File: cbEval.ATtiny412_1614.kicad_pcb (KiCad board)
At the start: 2 copper layers, 35 x 109 mm, 50 parts, among them J1 Bergstik-II_3, J10 Socket.Hor.2x5.6-5535512-4, J11 Bergstik-II_3, J12 Bergstik-II_3, J13 Bergstik-II_6, J14 Bergstik-II_6, J15 Bergstik-II_6, J16 Bergstik-II_3, J17 Bergstik-II_6, J18 Bergstik-II_3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

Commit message: kleinere Änderungen
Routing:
- net /PA3: track 0.00 -> 19.0 mm
- net /PA2: track 0.00 -> 16.6 mm
- net /PA1: track 0.00 -> 13.2 mm
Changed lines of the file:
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@@
     (effects (font (size 1 1) (thickness 0.15)))
   )
+  (segment (start 144.145 93.98) (end 155.258146 93.98) (width 0.25) (layer "F.Cu") (net 43))
+  (segment (start 155.258146 93.98) (end 156.21 93.028146) (width 0.25) (layer "F.Cu") (net 43))
+  (segment (start 142.875 92.71) (end 144.145 93.98) (width 0.25) (layer "F.Cu") (net 43))
+  (segment (start 154.94 89.535) (end 154.24 89.535) (width 0.25) (layer "F.Cu") (net 43))
+  (segment (start 156.21 90.805) (end 154.94 89.535) (width 0.25) (layer "F.Cu") (net 43))
+  (segment (start 156.21 93.028146) (end 156.21 90.805) (width 0.25) (layer "F.Cu") (net 43))
+  (segment (start 142.875 90.17) (end 145.40452 92.69952) (width 0.25) (layer "F.Cu") (net 44))
+  (segment (start 155.268626 92.69952) (end 155.575 92.393146) (width 0.25) (layer "F.Cu") (net 44))
+  (segment (start 155.575 92.393146) (end 155.575 91.165) (width 0.25) (layer "F.Cu") (net 44))
+  (segment (start 145.40452 92.69952) (end 155.268626 92.69952) (width 0.25) (layer "F.Cu") (net 44))
+  (segment (start 155.215 90.805) (end 154.24 90.805) (width 0.25) (layer "F.Cu") (net 44))
+  (segment (start 155.575 91.165) (end 155.215 90.805) (width 0.25) (layer "F.Cu") (net 44))
+  (segment (start 151.11952 91.42952) (end 151.765 92.075) (width 0.25) (layer "F.Cu") (net 45))
+  (segment (start 151.765 92.075) (end 154.24 92.075) (width 0.25) (layer "F.Cu") (net 45))
+  (segment (start 146.67452 91.42952) (end 151.11952 91.42952) (width 0.25) (layer "F.Cu") (net 45))
+  (segment (start 142.875 87.63) (end 146.67452 91.42952) (width 0.25) (layer "F.Cu") (net 45))
 )

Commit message: BOM erstellt und kleinere Korrekturen
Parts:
- added R10: 10k, Resistor_SMD:R_0805_2012Metric, F.Cu at (145.4, 135.3)
- added R11: 10k, Resistor_SMD:R_0805_2012Metric, F.Cu at (148.0, 135.3)
- added R12: 10k, Resistor_SMD:R_0805_2012Metric, F.Cu at (131.1, 127.0)
- added R13: 10k, Resistor_SMD:R_0805_2012Metric, F.Cu at (138.4, 131.2)
- added R14: 10k, Resistor_SMD:R_0805_2012Metric, F.Cu at (139.1, 135.3)
- added R15: 10k, Resistor_SMD:R_0805_2012Metric, F.Cu at (151.8, 127.0)
- added R9: 10k, Resistor_SMD:R_0805_2012Metric, F.Cu at (142.9, 135.3)
- moved J12 1.27 mm to (142.9, 131.4)
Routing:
- net /PA4: track 0.00 -> 18.9 mm
- net PB3: track 0.00 -> 8.26 mm
- net /PB0: track 0.00 -> 8.26 mm
- net PB2: track 0.00 -> 7.73 mm
- net /PB1: track 0.00 -> 7.73 mm

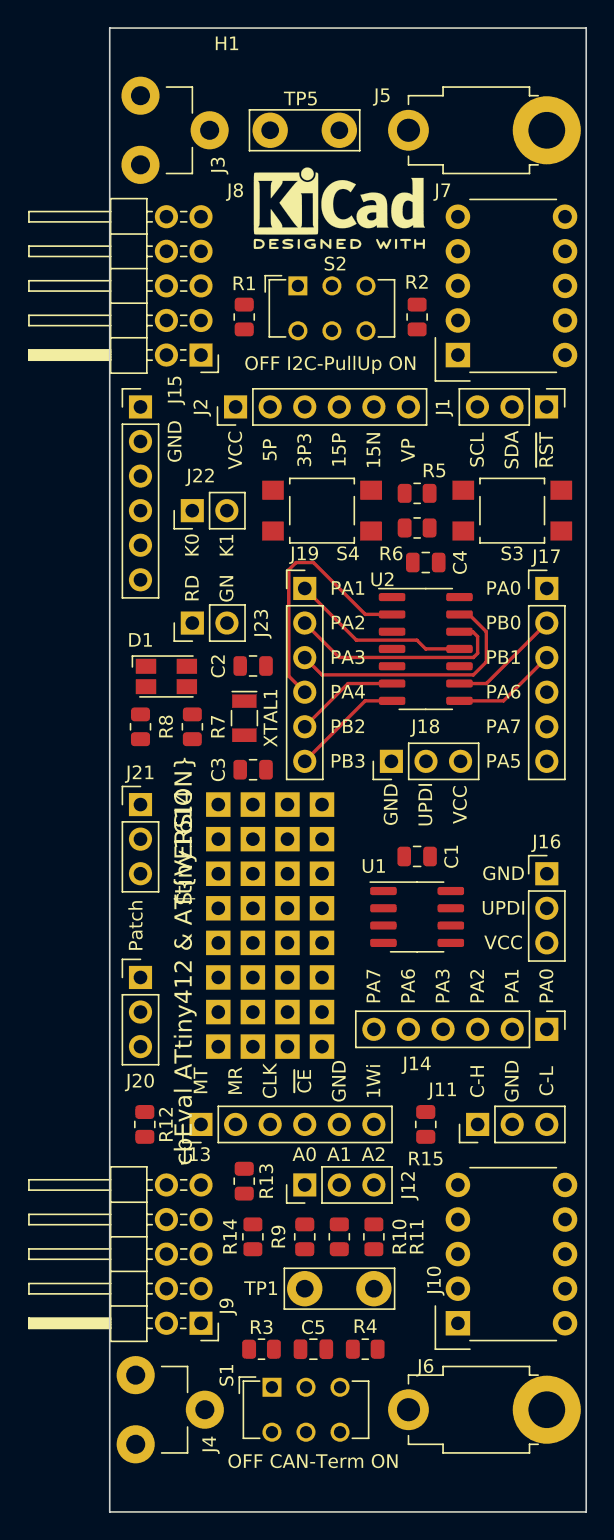
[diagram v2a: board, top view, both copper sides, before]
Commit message: Bus-Stecker ersetzt, Poti hinzugefügt
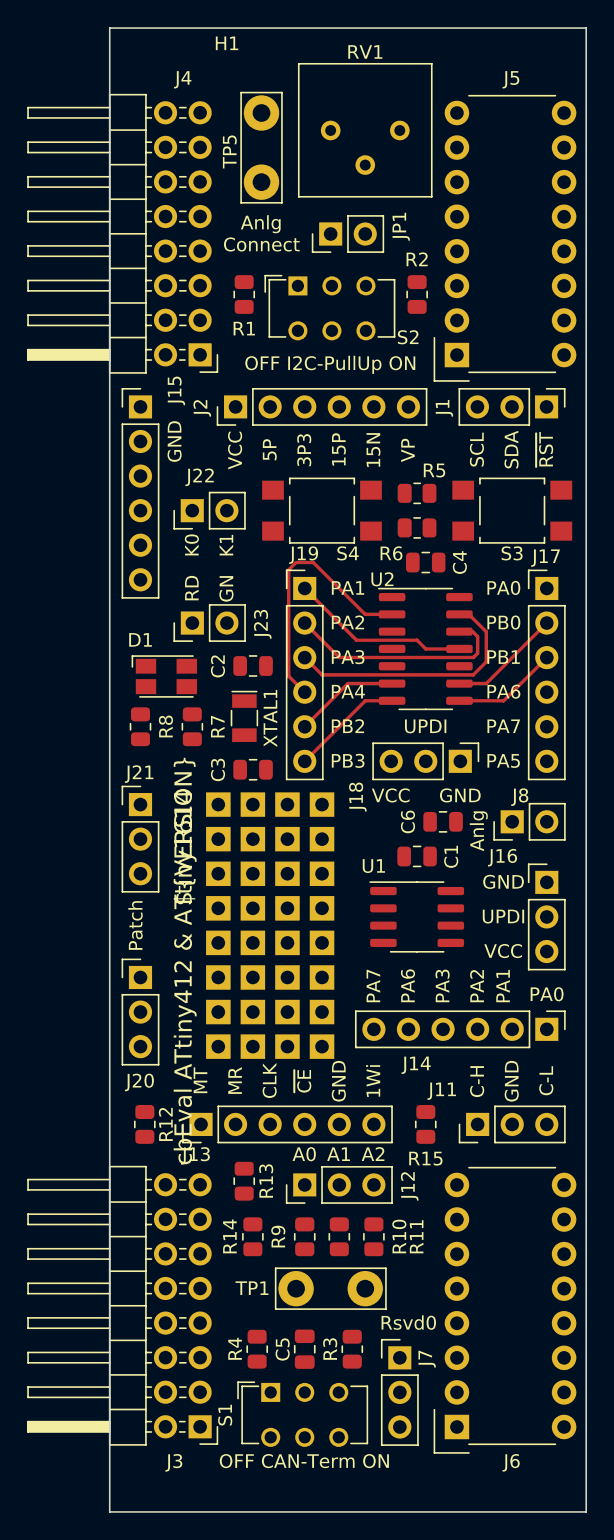
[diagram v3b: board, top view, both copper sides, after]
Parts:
- removed J10: Socket.Hor.2x5.6-5535512-4, BTech.Connector.AMPMODU-ModII:Socket.Hor.2x5.6-5535512-4
- removed J9: Header.Hor.2x5.9-103326-0-05, Connector_PinHeader_2.54mm:PinHeader_2x05_P2.54mm_Horizontal
- removed MP1: KiCAD-Logo2.5mm.SilkScreen, Symbol:KiCad-Logo2_5mm_SilkScreen
- added C6: 33n, Capacitor_SMD:C_0805_2012Metric, F.Cu at (153.0, 104.8)
- added JP1: Bergstik-II_2, Connector_PinHeader_2.54mm:PinHeader_1x02_P2.54mm_Vertical, F.Cu at (144.8, 61.6)
- added RV1: 4k7, Potentiometer_THT:Potentiometer_Bourns_3386P_Vertical, F.Cu at (144.8, 54.0)
- J3, J4: value Keystone.4918 -> Header.Hor.2x8.9-103326-0-08; footprint BTech.Connector.QuickConnect:Keystone.4918 -> Connector_PinHeader_2.54mm:PinHeader_2x08_P2.54mm_Horizontal
- J5, J6: value Keystone.3571 -> Socket.Hor.2x8.1-5535512-8; footprint BTech.Connector.QuickConnect:Keystone.3571 -> BTech.Connector.AMPMODU-ModII:Socket.Hor.2x5.6-5535512-4
- J7: value Socket.Hor.2x5.6-5535512-4 -> Bergstik-II_3; footprint BTech.Connector.AMPMODU-ModII:Socket.Hor.2x5.6-5535512-4 -> Connector_PinHeader_2.54mm:PinHeader_1x03_P2.54mm_Vertical
- J8: value Header.Hor.2x5.9-103326-0-05 -> Bergstik-II_2; footprint Connector_PinHeader_2.54mm:PinHeader_2x05_P2.54mm_Horizontal -> Connector_PinHeader_2.54mm:PinHeader_1x02_P2.54mm_Vertical
- moved J3 95.3 mm to (135.2, 149.2), turned to 180 degrees
- moved J7 79.7 mm to (149.9, 144.1)
- moved J4 77.6 mm to (135.2, 70.5), turned to 180 degrees
- moved J8 41.2 mm to (158.1, 104.8), turned to 90 degrees
- moved J5 10.9 mm to (161.9, 62.9)
- moved J6 8.98 mm to (161.9, 141.6)
- moved R4 7.94 mm to (139.4, 143.5), turned to -90 degrees
- moved R3 6.67 mm to (146.4, 143.5), turned to -90 degrees
- moved TP5 5.85 mm to (139.7, 52.7), turned to -90 degrees
- moved J18 5.06 mm to (154.3, 100.3), turned to -90 degrees
- moved R1 1.65 mm to (138.4, 66.0)
- moved R2 1.65 mm to (151.1, 66.0)
- moved J16 0.64 mm to (160.7, 109.2)
- moved C5 0.63 mm to (142.9, 143.5), turned to -90 degrees
- moved TP1 0.63 mm to (142.2, 139.1)
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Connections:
- J1 pad 1: /~RESET -> +VDC
- J4 pad 1: GND -> VCC
- J5 pad 1: GND -> VCC
- J7 pad 1: VCC -> /Reserved0
- J7 pad 2: VCC -> GND
- J7 pad 3: +5V -> /Reserved1
- J8 pad 1: VCC -> Net-(J8-Pad1)
- J8 pad 2: VCC -> Net-(J8-Pad1)
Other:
- board text added: "Anlg"
- board text added: "Anlg Connect"
- board text added: "Rsvd0"

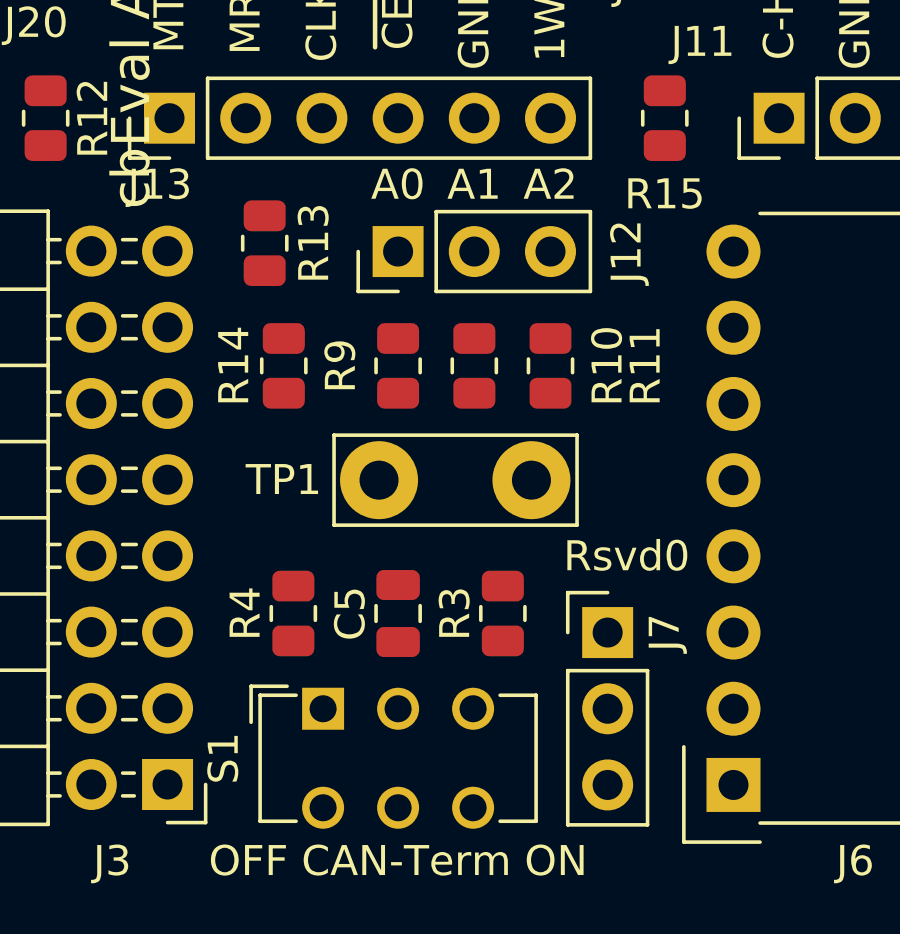
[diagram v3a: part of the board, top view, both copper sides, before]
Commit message: 1Wire-Terminierung hinzugefügt, BOM erneuert
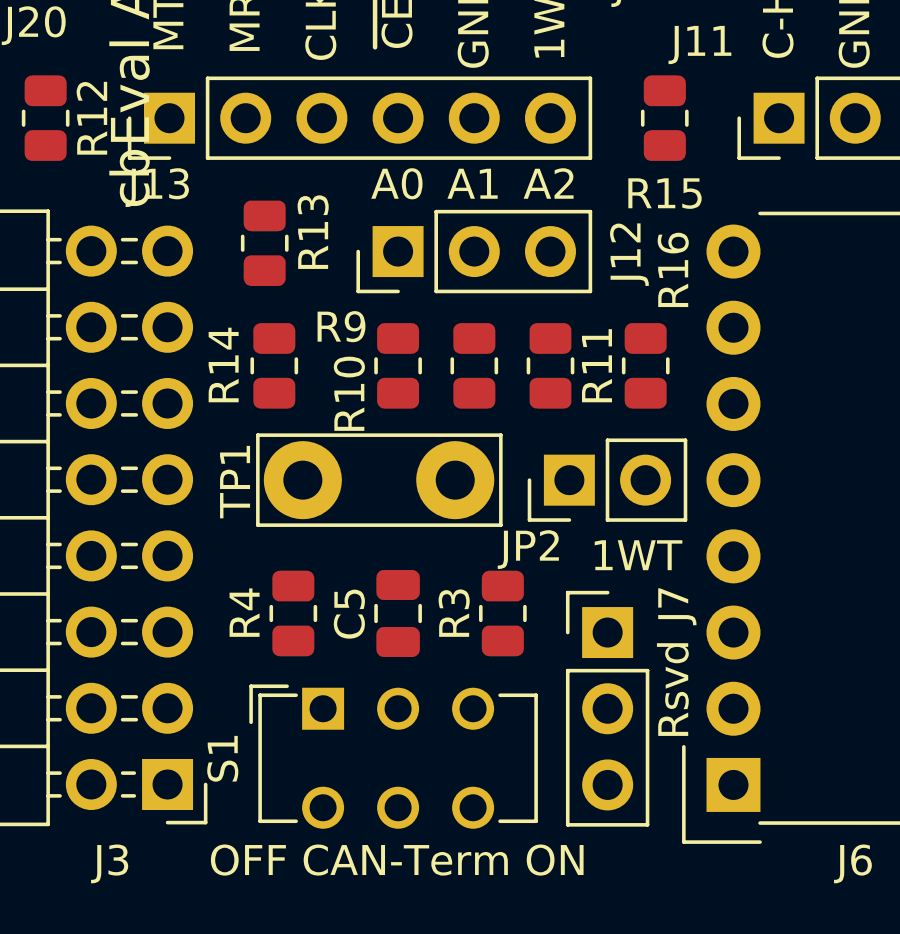
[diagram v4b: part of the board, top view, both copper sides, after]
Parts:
- added JP2: Bergstik-II_2, Connector_PinHeader_2.54mm:PinHeader_1x02_P2.54mm_Vertical, F.Cu at (148.6, 139.1)
- added R16: 4k7, Resistor_SMD:R_0805_2012Metric, F.Cu at (151.1, 135.3)
- moved TP1 2.54 mm to (139.7, 139.1)
- moved R14 0.32 mm to (138.7, 135.3)
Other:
- board text added: "1WT"
- board text added: "Rsvd"
- board text removed: "Rsvd0"
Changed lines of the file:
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@@
   (net 55 "Net-(J22-Pad2)")
   (net 56 "/Reserved0")
-  (net 57 "Net-(J8-Pad1)")
+  (net 57 "Net-(C6-Pad1)")
   (net 58 "Net-(JP1-Pad1)")
+  (net 59 "Net-(JP2-Pad2)")
   (footprint "BTech.Housing:Camdenboss.CIME.E.BE3500S.1x" locked (layer "F.Cu")
     (at 146.05 100.965)
@@
   )
   (footprint "Resistor_SMD:R_0805_2012Metric" (layer "F.Cu")
-    (at 139.065 135.255 90)
+    (at 138.7475 135.255 90)
     (descr "Resistor SMD 0805 (2012 Metric), square (rectangular) end terminal, IPC_7351 nominal, (Body size source: IPC-SM-782 page 72, https://www.pcb-3d.com/wordpress/wp-content/uploads/ipc-sm-782a_amendment_1_and_2.pdf), generated with kicad-footprint-generator")
     (tags "resistor")
@@
     (property "Tolerance" "1%")
     (attr smd)
-    (fp_text reference "R9" (at 0 1.905 90) (layer "F.SilkS")
+    (fp_text reference "R9" (at -1.27 1.905 180) (layer "F.SilkS")
       (effects (font (size 1 1) (thickness 0.15)))
     )
@@
     )
   )
+  (footprint "Resistor_SMD:R_0805_2012Metric" (layer "F.Cu")
+    (at 151.13 135.255 90)
+    (descr "Resistor SMD 0805 (2012 Metric), square (rectangular) end terminal, IPC_7351 nominal, (Body size source: IPC-SM-782 page 72, https://www.pcb-3d.com/wordpress/wp-content/uploads/ipc-sm-782a_amendment_1_and_2.pdf), generated with kicad-footprint-generator")
+    (tags "resistor")
+    (property "ID" "RC0805FR-074K7L")
+    (property "Package" "0805")
+    (property "Power" "0W125")
+    (property "Sheetfile" "cbEval.ATtiny412_1614.kicad_sch")
+    (property "Sheetname" "")
+    (property "TK" "TK100")
+    (property "Tolerance" "1%")
+    (attr smd)
+    (fp_text reference "R16" (at 3.175 0.9525 90) (layer "F.SilkS")
+      (effects (font (size 1 1) (thickness 0.15)))
+    )
+    (fp_text value "4k7" (at 0 1.65 90) (layer "F.Fab") hide
+      (effects (font (size 1 1) (thickness 0.15)))
+    )
+    (fp_text user "${REFERENCE}" (at 0 0 90) (layer "F.Fab")
+      (effects (font (size 0.5 0.5) (thickness 0.08)))
+    )
+    (fp_line (start -0.227064 -0.735) (end 0.227064 -0.735) (layer "F.SilkS") (width 0.12))
+    (fp_line (start -0.227064 0.735) (end 0.227064 0.735) (layer "F.SilkS") (width 0.12))
+    (fp_line (start -1.68 0.95) (end -1.68 -0.95) (layer "F.CrtYd") (width 0.05))
+    (fp_line (start 1.68 0.95) (end -1.68 0.95) (layer "F.CrtYd") (width 0.05))
+    (fp_line (start 1.68 -0.95) (end 1.68 0.95) (layer "F.CrtYd") (width 0.05))
+    (fp_line (start -1.68 -0.95) (end 1.68 -0.95) (layer "F.CrtYd") (width 0.05))
+    (fp_line (start -1 -0.625) (end 1 -0.625) (layer "F.Fab") (width 0.1))
+    (fp_line (start 1 -0.625) (end 1 0.625) (layer "F.Fab") (width 0.1))
+    (fp_line (start -1 0.625) (end -1 -0.625) (layer "F.Fab") (width 0.1))
+    (fp_line (start 1 0.625) (end -1 0.625) (layer "F.Fab") (width 0.1))
+    (pad "1" smd roundrect (at -0.9125 0 90) (locked) (size 1.025 1.4) (layers "F.Cu" "F.Paste" "F.Mask") (roundrect_rratio 0.243902)
+      (net 59 "Net-(JP2-Pad2)") (pintype "passive"))
+    (pad "2" smd roundrect (at 0.9125 0 90) (locked) (size 1.025 1.4) (layers "F.Cu" "F.Paste" "F.Mask") (roundrect_rratio 0.243902)
+      (net 7 "/One-Wire") (pintype "passive"))
+    (model "${KICAD6_3DMODEL_DIR}/Resistor_SMD.3dshapes/R_0805_2012Metric.wrl"
+      (offset (xyz 0 0 0))
+      (scale (xyz 1 1 1))
+      (rotate (xyz 0 0 0))
+    )
+  )
   (footprint "Connector_PinHeader_2.54mm:PinHeader_1x02_P2.54mm_Vertical" (layer "F.Cu")
     (at 144.78 61.595 90)
@@
       (net 58 "Net-(JP1-Pad1)") (pinfunction "A") (pintype "passive"))
     (pad "2" thru_hole oval (at 0 2.54 90) (locked) (size 1.7 1.7) (drill 1) (layers *.Cu *.Mask)
-      (net 57 "Net-(J8-Pad1)") (pinfunction "B") (pintype "passive"))
+      (net 57 "Net-(C6-Pad1)") (pinfunction "B") (pintype "passive"))
     (model "${KICAD6_3DMODEL_DIR}/Connector_PinHeader_2.54mm.3dshapes/PinHeader_1x02_P2.54mm_Vertical.wrl"
       (offset (xyz 0 0 0))
@@
   )
   (footprint "TestPoint:TestPoint_Bridge_Pitch5.08mm_Drill1.3mm" (layer "F.Cu")
-    (at 142.24 139.065)
+    (at 139.7 139.065)
     (descr "wire loop as test point, pitch 5.08mm, hole diameter 1.3mm, wire diameter 1.0mm")
     (tags "test point wire loop")
@@
     (property "Usage" "Meas GND")
     (attr through_hole)
-    (fp_text reference "TP1" (at -3.175 0) (layer "F.SilkS")
+    (fp_text reference "TP1" (at -2.2225 0 90) (layer "F.SilkS")
       (effects (font (size 1 1) (thickness 0.15)))
     )
@@
     (property "Usage" "Reserved")
     (attr through_hole)
-    (fp_text reference "J7" (at 1.905 0 90) (layer "F.SilkS")
+    (fp_text reference "J7" (at 2.2225 -0.9525 270) (layer "F.SilkS")
       (effects (font (size 1 1) (thickness 0.15)))
     )
@@
     (property "Tolerance" "1%")
     (attr smd)
-    (fp_text reference "R11" (at 0 -3.175 90) (layer "F.SilkS")
+    (fp_text reference "R11" (at 0 -1.5875 90) (layer "F.SilkS")
       (effects (font (size 1 1) (thickness 0.15)))
     )
@@
     (property "Tolerance" "1%")
     (attr smd)
-    (fp_text reference "R13" (at 0 -1.65 90) (layer "F.SilkS")
+    (fp_text reference "R13" (at -0.3575 -1.65 90) (layer "F.SilkS")
       (effects (font (size 1 1) (thickness 0.15)))
     )
@@
     (fp_line (start 1 -0.625) (end 1 0.625) (layer "F.Fab") (width 0.1))
     (pad "1" smd roundrect (at -0.95 0 180) (locked) (size 1 1.45) (layers "F.Cu" "F.Paste" "F.Mask") (roundrect_rratio 0.25)
-      (net 57 "Net-(J8-Pad1)") (pintype "passive"))
+      (net 57 "Net-(C6-Pad1)") (pintype "passive"))
     (pad "2" smd roundrect (at 0.95 0 180) (locked) (size 1 1.45) (layers "F.Cu" "F.Paste" "F.Mask") (roundrect_rratio 0.25)
       (net 2 "GND") (pintype "passive"))
@@
     (fp_line (start 1.27 3.81) (end -1.27 3.81) (layer "F.Fab") (width 0.1))
     (pad "1" thru_hole rect (at 0 0 90) (locked) (size 1.7 1.7) (drill 1) (layers *.Cu *.Mask)
-      (net 57 "Net-(J8-Pad1)") (pinfunction "A1") (pintype "passive"))
+      (net 57 "Net-(C6-Pad1)") (pinfunction "A1") (pintype "passive"))
     (pad "2" thru_hole oval (at 0 2.54 90) (locked) (size 1.7 1.7) (drill 1) (layers *.Cu *.Mask)
-      (net 57 "Net-(J8-Pad1)") (pinfunction "A2") (pintype "passive"))
+      (net 57 "Net-(C6-Pad1)") (pinfunction "A2") (pintype "passive"))
     (model "${KICAD6_3DMODEL_DIR}/Connector_PinHeader_2.54mm.3dshapes/PinHeader_1x02_P2.54mm_Vertical.wrl"
       (offset (xyz 0 0 0))
@@
     )
   )
+  (footprint "Connector_PinHeader_2.54mm:PinHeader_1x02_P2.54mm_Vertical" (layer "F.Cu")
+    (at 148.585 139.065 90)
+    (descr "Through hole straight pin header, 1x02, 2.54mm pitch, single row")
+    (tags "Through hole pin header THT 1x02 2.54mm single row")
+    (property "ID" "68000-102HLF")
+    (property "Package" "1x2-2.54")
+    (property "Sheetfile" "cbEval.ATtiny412_1614.kicad_sch")
+    (property "Sheetname" "")
+    (property "Usage" "1Wire Term")
+    (attr through_hole)
+    (fp_text reference "JP2" (at -2.2225 -1.265 180) (layer "F.SilkS")
+      (effects (font (size 1 1) (thickness 0.15)))
+    )
+    (fp_text value "Bergstik-II_2" (at 0 4.87 90) (layer "F.Fab") hide
+      (effects (font (size 1 1) (thickness 0.15)))
+    )
+    (fp_text user "${REFERENCE}" (at 0 1.27) (layer "F.Fab")
+      (effects (font (size 1 1) (thickness 0.15)))
+    )
+    (fp_line (start -1.33 1.27) (end -1.33 3.87) (layer "F.SilkS") (width 0.12))
+    (fp_line (start -1.33 0) (end -1.33 -1.33) (layer "F.SilkS") (width 0.12))
+    (fp_line (start -1.33 -1.33) (end 0 -1.33) (layer "F.SilkS") (width 0.12))
+    (fp_line (start -1.33 3.87) (end 1.33 3.87) (layer "F.SilkS") (width 0.12))
+    (fp_line (start 1.33 1.27) (end 1.33 3.87) (layer "F.SilkS") (width 0.12))
+    (fp_line (start -1.33 1.27) (end 1.33 1.27) (layer "F.SilkS") (width 0.12))
+    (fp_line (start -1.8 -1.8) (end -1.8 4.35) (layer "F.CrtYd") (width 0.05))
+    (fp_line (start -1.8 4.35) (end 1.8 4.35) (layer "F.CrtYd") (width 0.05))
+    (fp_line (start 1.8 4.35) (end 1.8 -1.8) (layer "F.CrtYd") (width 0.05))
+    (fp_line (start 1.8 -1.8) (end -1.8 -1.8) (layer "F.CrtYd") (width 0.05))
+    (fp_line (start 1.27 -1.27) (end 1.27 3.81) (layer "F.Fab") (width 0.1))
+    (fp_line (start -1.27 3.81) (end -1.27 -0.635) (layer "F.Fab") (width 0.1))
+    (fp_line (start -1.27 -0.635) (end -0.635 -1.27) (layer "F.Fab") (width 0.1))
+    (fp_line (start -0.635 -1.27) (end 1.27 -1.27) (layer "F.Fab") (width 0.1))
+    (fp_line (start 1.27 3.81) (end -1.27 3.81) (layer "F.Fab") (width 0.1))
+    (pad "1" thru_hole rect (at 0 0 90) (locked) (size 1.7 1.7) (drill 1) (layers *.Cu *.Mask)
+      (net 1 "VCC") (pinfunction "A") (pintype "passive"))
+    (pad "2" thru_hole oval (at 0 2.54 90) (locked) (size 1.7 1.7) (drill 1) (layers *.Cu *.Mask)
+      (net 59 "Net-(JP2-Pad2)") (pinfunction "B") (pintype "passive"))
+    (model "${KICAD6_3DMODEL_DIR}/Connector_PinHeader_2.54mm.3dshapes/PinHeader_1x02_P2.54mm_Vertical.wrl"
+      (offset (xyz 0 0 0))
+      (scale (xyz 1 1 1))
+      (rotate (xyz 0 0 0))
+    )
+  )
   (footprint "Connector_PinHeader_2.54mm:PinHeader_1x06_P2.54mm_Vertical" (layer "F.Cu")
     (at 130.81 74.295)
@@
     (property "Tolerance" "1%")
     (attr smd)
-    (fp_text reference "R10" (at 0 -4.445 90) (layer "F.SilkS")
+    (fp_text reference "R10" (at 0.9525 4.1275 90) (layer "F.SilkS")
       (effects (font (size 1 1) (thickness 0.15)))
     )
@@
     (effects (font (size 1 1) (thickness 0.15)))
   )
-  (gr_text "Rsvd0" (at 150.495 141.605) (layer "F.SilkS")
+  (gr_text "1WT" (at 150.8125 141.605) (layer "F.SilkS")
     (effects (font (size 1 1) (thickness 0.15)))
   )
@@
     (effects (font (size 1 1) (thickness 0.15)))
   )
+  (gr_text "Rsvd" (at 152.0825 146.05 90) (layer "F.SilkS")
+    (effects (font (size 1 1) (thickness 0.15)))
+  )

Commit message: PowerBus-Belegung V1.1
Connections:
- net /SPI-~CE renamed /SPI-~{CE}
- J4 pad 3: +5V -> +3V3
- J4 pad 4: +3V3 -> +15V
- J4 pad 5: +15V -> +5V
- J5 pad 3: +5V -> +3V3
- J5 pad 4: +3V3 -> +15V
- J5 pad 5: +15V -> +5V
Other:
- board text added: "~{CE}"
- board text added: "~{RST}"
- board text removed: "~CE"
- board text removed: "~RST"
